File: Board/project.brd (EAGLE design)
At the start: 106.3 x 80 mm, 18 parts, among them U1 ATMEGA328P_PDIP

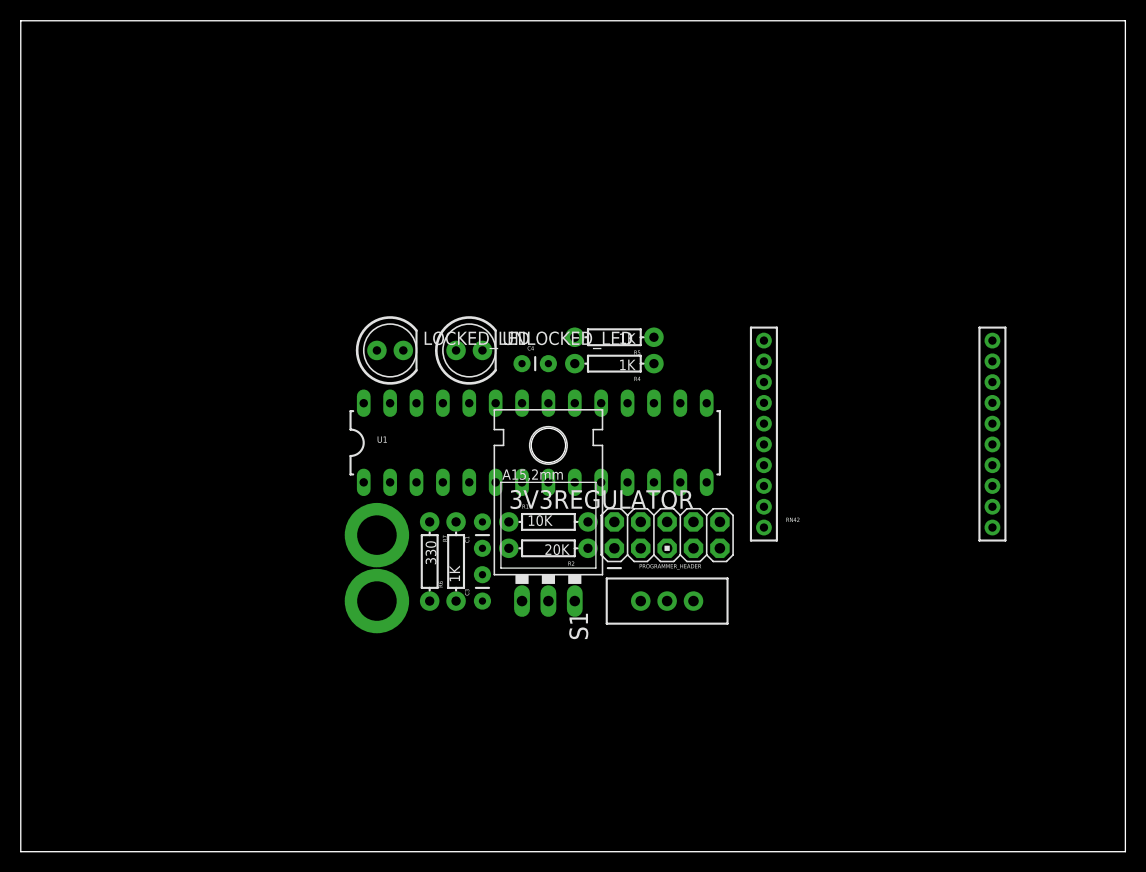
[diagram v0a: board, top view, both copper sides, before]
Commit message: Changed some pins for better routing, passes DRC now.
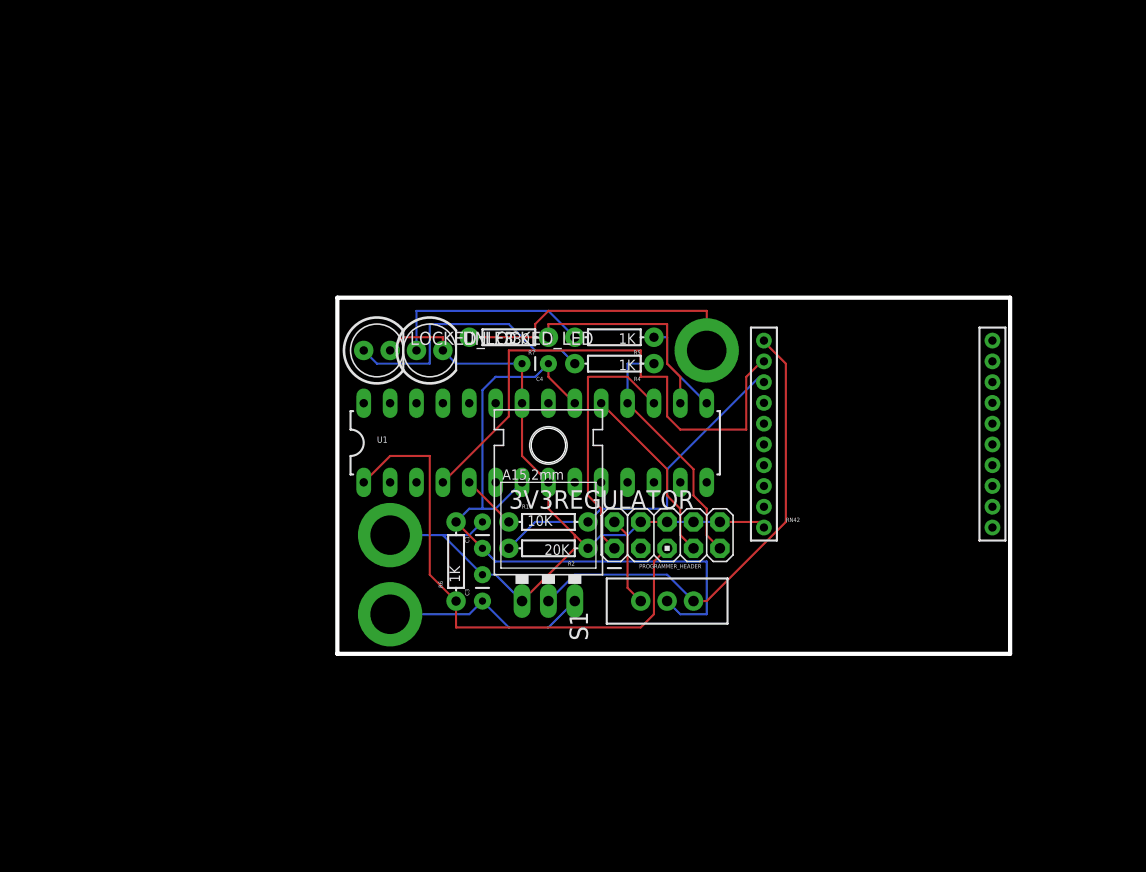
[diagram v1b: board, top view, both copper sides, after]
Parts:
- added JP3: M01-SMTSO-256-ET, SparkFun-Connectors:SMTSO-256-ET
- moved JP1 36.4 mm to (66.0, 48.3)
- moved R7 22.9 mm to (47.0, 49.5), turned to 180 degrees
- moved UNLOCKED_LED 3.81 mm to (39.4, 48.3)
- moved C4 2.54 mm to (50.8, 47.0), turned to 180 degrees
- moved JP2 1.80 mm to (35.6, 22.9)
- moved LOCKED_LED 1.27 mm to (34.3, 48.3)
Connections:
- removed net N$4: R7.P$1, U1.6
- new net N$3: R7.P$1, U1.16
- net GND: now also JP3.P$1
- net N$2: now also U1.15; no longer U1.14
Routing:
- net GND: track 0.00 -> 81.8 mm
- net UC_VCC: track 0.00 -> 66.7 mm
- net BT_RX: track 0.00 -> 52.4 mm
- net RESET: track 0.00 -> 51.4 mm
- net 3V3: track 0.00 -> 47.5 mm
- net N$1: track 0.00 -> 33.9 mm
- net MI_TRANSMITTER: track 0.00 -> 28.5 mm
- net N$5: track 0.00 -> 26.2 mm
- net MOSI: track 0.00 -> 25.0 mm
- net MISO: track 0.00 -> 24.0 mm
- net N$3: track 0.00 -> 20.8 mm
- net BAT_IN: track 0.00 -> 20.4 mm
- net N$6: track 0.00 -> 20.1 mm
- net SCK: track 0.00 -> 17.7 mm
- net N$2: track 0.00 -> 9.20 mm
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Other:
- board size 106.3 x 80 mm -> 64.8 x 34.3 mm

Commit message: Better board layout, everything that needs to be should be connected, passes DRC.
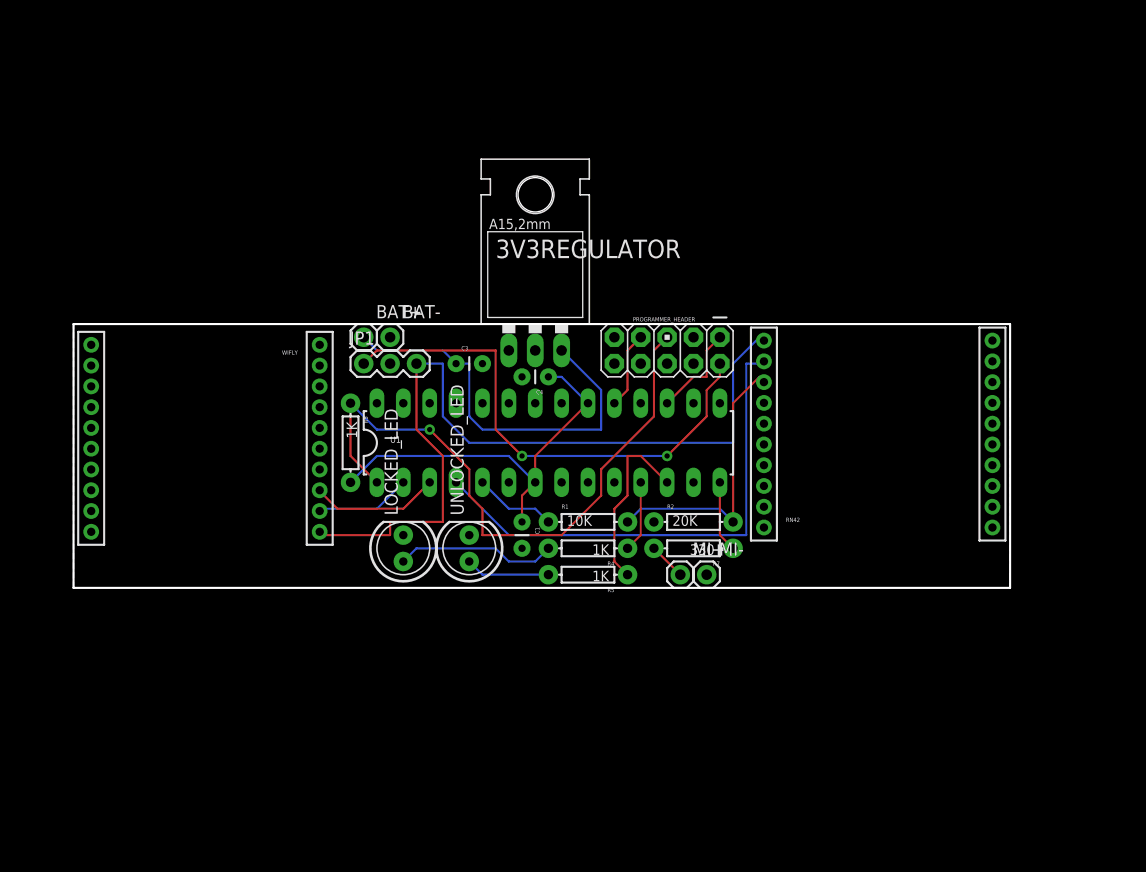
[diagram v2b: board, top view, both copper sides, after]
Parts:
- removed JP2, JP3: M01-SMTSO-256-ET, SparkFun-Connectors:SMTSO-256-ET
- removed S1: (no value), SparkFun-Electromechanical:SWITCH-SPDT
- added BAT+, BAT-, MI+, MI-: M01PTH, SparkFun-Connectors:1X01
- added WIFLY: XBEE-1B1, SparkFun-RF:XBEE-1
- JP1: value M01-SMTSO-256-ET -> JUMPER-3PTH; device SparkFun-Connectors:SMTSO-256-ET -> SparkFun-Passives:1X03
- moved JP1 33.0 mm to (33.0, 47.0)
- moved R7 27.0 mm to (64.8, 29.2)
- moved 3V3REGULATOR 24.2 mm to (49.5, 52.1)
- moved C3 23.0 mm to (41.9, 47.0), turned to 0 degrees
- moved R5 23.0 mm to (54.6, 26.7)
- moved UNLOCKED_LED 19.4 mm to (43.2, 29.2), turned to 90 degrees
- moved LOCKED_LED 19.2 mm to (36.8, 29.2), turned to 90 degrees
- moved R4 18.0 mm to (54.6, 29.2)
- moved PROGRAMMER_HEADER 17.8 mm to (62.2, 48.3), turned to 270 degrees
- moved R6 15.3 mm to (31.8, 39.4), turned to 270 degrees
- moved R2 14.2 mm to (64.8, 31.8), turned to 0 degrees
- moved C1 4.58 mm to (48.3, 31.8), turned to 270 degrees
- moved R1 3.81 mm to (54.6, 31.8)
- moved C4 1.27 mm to (50.8, 45.7)
- moved U1 1.27 mm to (50.8, 39.4)
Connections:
- new net N$4: R4.P$1, U1.11
- new net N$7: R7.P$1, U1.14
- new net WIFLY_RX: U1.2, WIFLY.2
- new net WIFLY_TX: U1.3, WIFLY.3
- net 3V3: now also JP1.3, WIFLY.1; no longer S1.3
- net 5V: now also JP1.1; no longer S1.1
- net BAT_IN: now also BAT+.1; no longer JP2.P$1
- net GND: now also BAT-.1, MI-.1, WIFLY.10; no longer JP3.P$1
- net MISO: no longer R4.P$1, U1.18
- net MI_TRANSMITTER: now also MI+.1; no longer JP1.P$1
- net N$2: now also U1.12; no longer U1.15
- net N$3: no longer R7.P$1
- net UC_VCC: no longer S1.2
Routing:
- net GND: track 81.8 -> 0.00 mm
- net 5V: track 8.67 -> 49.4 mm, vias 0 -> 2
- net 3V3: track 47.5 -> 77.9 mm
- net UC_VCC: track 66.7 -> 38.8 mm
- net MI_TRANSMITTER: track 28.5 -> 3.59 mm
- net MISO: track 24.0 -> 0.00 mm
- net N$3: track 20.8 -> 0.00 mm
- net BAT_IN: track 20.4 -> 38.7 mm
- net MOSI: track 25.0 -> 9.20 mm
- net WIFLY_TX: track 0.00 -> 12.4 mm
- net N$6: track 20.1 -> 8.15 mm
- net N$5: track 26.2 -> 15.5 mm
- net SCK: track 17.7 -> 7.40 mm
- net WIFLY_RX: track 0.00 -> 9.16 mm
- net RESET: track 51.4 -> 60.5 mm, vias 0 -> 1
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- added copper zone on layer 1, net GND
- added copper zone on layer 16, net GND
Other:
- board size 64.8 x 34.3 mm -> 90.2 x 25.4 mm

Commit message: Layout actually works, added silkscreen.
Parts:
- removed JP1: JUMPER-3PTH, SparkFun-Passives:1X03
- added JP2: JUMPER-3-OLDPTH, SparkFun-Passives:1X03
- moved BAT+ 34.3 mm to (67.3, 48.3)
- moved BAT- 31.8 mm to (67.3, 50.8)
- moved 3V3REGULATOR 14.0 mm to (35.6, 50.8)
- moved PROGRAMMER_HEADER 5.24 mm to (57.1, 49.5), turned to 90 degrees
- moved MI+ 2.54 mm to (66.0, 26.7)
- moved MI- 2.54 mm to (63.5, 26.7)
- moved LOCKED_LED 2.54 mm to (34.3, 29.2)
- moved C4 1.80 mm to (49.5, 47.0)
- moved UNLOCKED_LED 1.27 mm to (41.9, 29.2)
- turned C1 to 180 degrees
- turned C3 to 90 degrees
- turned R2 to 180 degrees
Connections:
- net 3V3: now also 3V3REGULATOR.OUT, JP2.1; no longer 3V3REGULATOR.GND, JP1.3
- net 5V: now also JP2.3; no longer JP1.1
- net BAT_IN: now also 3V3REGULATOR.IN; no longer 3V3REGULATOR.OUT
- net GND: now also 3V3REGULATOR.GND; no longer 3V3REGULATOR.IN
- net UC_VCC: now also JP2.2
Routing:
- net 5V: track 49.4 -> 2.54 mm, vias 2 -> 0
- net RESET: track 60.5 -> 38.9 mm
- net BT_RX: track 48.3 -> 36.7 mm, vias 0 -> 1
- net MOSI: track 9.20 -> 17.0 mm
- net UC_VCC: track 38.8 -> 46.4 mm, vias 0 -> 1
- net N$2: track 17.3 -> 13.0 mm
- net 3V3: track 77.9 -> 75.3 mm
- net MI_TRANSMITTER: track 3.59 -> 6.13 mm
- net N$1: track 26.9 -> 24.7 mm
- net BAT_IN: track 38.7 -> 40.8 mm, vias 0 -> 1
- net WIFLY_RX: track 9.16 -> 11.0 mm
- net WIFLY_TX: track 12.4 -> 13.9 mm
- net N$5: track 15.5 -> 17.0 mm
- net N$6: track 8.15 -> 9.42 mm
- net SCK: track 7.40 -> 6.13 mm
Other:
- board size 90.2 x 25.4 mm -> 90.2 x 26.7 mm
- board text added: "+"
- board text added: "-"
- board text added: "3.3V"
- board text added: "5V"
- board text added: "BAT+"
- board text added: "BAT-"
- board text added: "PhoneKey"
- board text added: "RN42"
- board text added: "WiFly"

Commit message: Updated board.
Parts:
- IC1: value V_REG_LD1117VXX -> (none)
- moved C4 4.02 mm to (53.3, 45.7)
- moved C1 2.54 mm to (45.7, 31.8), turned to 0 degrees
- moved C3 1.80 mm to (43.2, 48.3), turned to 270 degrees
- moved JP2 1.27 mm to (43.2, 50.8)
- renumbered 3V3REGULATOR to IC1
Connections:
- net MISO: now also U1.18
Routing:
- net 3V3: track 75.3 -> 88.4 mm, vias 0 -> 1
- net MISO: track 0.00 -> 6.88 mm
- net UC_VCC: track 46.4 -> 50.0 mm, vias 1 -> 0
- net MOSI: track 17.0 -> 20.6 mm
- net BAT_IN: track 40.8 -> 38.7 mm, vias 1 -> 0
- net N$1: track 24.7 -> 26.5 mm
- net BT_RX: track 36.7 -> 38.5 mm
- net 5V: track 2.54 -> 3.81 mm
- net SCK: track 6.13 -> 6.88 mm
